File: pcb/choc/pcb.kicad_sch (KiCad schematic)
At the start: 144 parts, among them J1 MJ-4PP-9, J10 Conn_01x08_Female, J2 USB_C_Receptacle_USB2.0, J3 Conn_01x12_Female, J4 Conn_01x04_Female, J5 Conn_01x08_Female, J6 MJ-4PP-9, J7 USB_C_Receptacle_USB2.0, J8 Conn_01x12_Female, J9 Conn_01x04_Female, SW1 SW_PUSH, SW10 SW_PUSH, SW11 SW_PUSH, SW12 SW_PUSH, SW13 SW_PUSH, SW14 SW_PUSH, SW15 SW_PUSH, SW16 SW_PUSH, SW17 SW_PUSH, SW18 SW_PUSH, SW19 SW_PUSH, SW2 SW_PUSH, SW20 SW_PUSH, SW21 SW_PUSH, SW22 SW_PUSH, SW23 SW_PUSH, SW24 SW_PUSH, SW25 SW_PUSH, SW26 SW_PUSH, SW27 SW_PUSH, SW28 SW_PUSH, SW29 SW_PUSH, SW3 SW_PUSH, SW30 SW_PUSH, SW31 SW_PUSH, SW32 SW_PUSH, SW33 SW_PUSH, SW34 SW_PUSH, SW35 SW_PUSH, SW36 SW_PUSH, SW37 SW_PUSH, SW38 SW_PUSH, SW4 SW_PUSH, SW5 SW_PUSH, SW6 SW_PUSH, SW7 SW_PUSH, SW8 SW_PUSH, SW9 SW_PUSH, U1 rp2040-zero, U2 rp2040-zero, U3 roller, U4 roller

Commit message: draft 1
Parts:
- added BR1, BR2, BR3, BR4: MountingHole, zzkeeb:Hole_Breakaway-Tabs, symbol Mechanical:MountingHole
- added CIRQUE2, CIRQUE4: Conn_01x12_Female, zzkeeb:Connector_FPC-FFC-adapter-12pin, symbol zzkeeb:Pointing_Cirque
- CIRQUE1: renamed from J3; footprint (none) -> zzkeeb:Connector_FFC-FPC-vertical-12pin; symbol Connector:Conn_01x12_Female -> zzkeeb:Pointing_Cirque
- CIRQUE3: renamed from J8; footprint (none) -> zzkeeb:Connector_FFC-FPC-vertical-12pin; symbol Connector:Conn_01x12_Female -> zzkeeb:Pointing_Cirque
- DISP1: renamed from J5; footprint Connector_JST:JST_PH_S8B-PH-K_1x08_P2.00mm_Horizontal -> zzkeeb:Connector_JST_PH_S8B-PH-K_1x08_P2.00mm_Horizontal; symbol Connector:Conn_01x08_Female -> zzkeeb:Display_Waveshare
- DISP2: renamed from J10; footprint Connector_JST:JST_PH_S8B-PH-K_1x08_P2.00mm_Horizontal -> zzkeeb:Connector_JST_PH_S8B-PH-K_1x08_P2.00mm_Horizontal; symbol Connector:Conn_01x08_Female -> zzkeeb:Display_Waveshare
- I2C1: renamed from J4; symbol Connector:Conn_01x04_Female -> zzkeeb:Pointing_Circue-adapter
- I2C2: renamed from J9; symbol Connector:Conn_01x04_Female -> zzkeeb:Pointing_Circue-adapter
- LED1, LED10, LED11, LED12, LED13, LED14, LED15, LED16, LED17, LED18, LED19, LED2, LED20, LED21, LED22, LED23, LED24, LED25, LED26, LED27, LED28, LED29, LED3, LED30, LED31, LED32, LED33, LED34, LED35, LED36, LED37, LED38, LED4, LED5, LED6, LED7, LED8, LED9: symbol kbd:YS-SK6812MINI-E -> zzkeeb:LED_SK6812MINI-E
- MCU1: renamed from U1; symbol kleeb-mcu:rp2040-zero -> zzkeeb:MCU_rp2040-zero
- MCU2: renamed from U2; symbol kleeb-mcu:rp2040-zero -> zzkeeb:MCU_rp2040-zero
- SW1, SW10, SW11, SW12, SW13, SW14, SW15, SW16, SW17, SW18, SW19, SW2, SW20, SW21, SW22, SW23, SW24, SW25, SW26, SW27, SW28, SW29, SW3, SW30, SW31, SW32, SW33, SW34, SW35, SW36, SW37, SW38, SW4, SW5, SW6, SW7, SW8, SW9: value SW_PUSH -> Switch; symbol kbd:SW_PUSH -> zzkeeb:Switch
- TRRS1: renamed from J1; symbol kbd:MJ-4PP-9 -> Connector:AudioJack4
- TRRS2: renamed from J6; symbol kbd:MJ-4PP-9 -> Connector:AudioJack4
- renumbered U3 to ROLL1, U4 to ROLL2, J2 to USB1, J7 to USB2
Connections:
- net CS: now also CIRQUE1.10 (SS), MCU1.10 (9), CIRQUE2.10 (SS); no longer CIRQUE1.11 (Pin_11), MCU1.6 (5)
- net CS_r: now also CIRQUE3.10 (SS), MCU2.10 (9), CIRQUE4.10 (SS); no longer CIRQUE3.11 (Pin_11), MCU2.6 (5)
- net GND: now also TRRS1.R1, CIRQUE2.2 (GND); no longer TRRS1.C
- net GNDA: now also TRRS2.R1, CIRQUE4.2 (GND); no longer TRRS2.C
- net MISO/DC: now also CIRQUE1.11 (MISO), MCU1.13 (12), CIRQUE2.11 (MISO); no longer CIRQUE1.10 (Pin_10), MCU1.5 (4)
- net MISO/DC_r: now also CIRQUE3.11 (MISO), MCU2.13 (12), CIRQUE4.11 (MISO); no longer CIRQUE3.10 (Pin_10), MCU2.5 (4)
- net MOSI/SCL: now also MCU1.12 (11), CIRQUE2.4 (SCL), CIRQUE2.8 (MOSI); no longer MCU1.4 (3)
- net MOSI/SCL_r: now also MCU2.12 (11), CIRQUE4.4 (SCL), CIRQUE4.8 (MOSI); no longer MCU2.4 (3)
- net RST: now also MCU1.14 (13); no longer MCU1.7 (6)
- net RST_r: now also MCU2.14 (13); no longer MCU2.7 (6)
- net RX: now also TRRS1.T; no longer TRRS1.B
- net RX_r: now also TRRS2.T; no longer TRRS2.B
- net SCLK/SDA: now also MCU1.11 (10), CIRQUE2.12 (SCK), CIRQUE2.3 (SDA); no longer MCU1.3 (2)
- net SCLK/SDA_r: now also MCU2.11 (10), CIRQUE4.12 (SCK), CIRQUE4.3 (SDA); no longer MCU2.3 (2)
- net TX: now also TRRS1.S; no longer TRRS1.A
- net TX_r: now also TRRS2.S; no longer TRRS2.A
- net VCC: now also TRRS1.R2, CIRQUE2.1 (3V3); no longer TRRS1.D
- net VDD: now also TRRS2.R2, CIRQUE4.1 (3V3); no longer TRRS2.D
- net col0: now also MCU1.3 (2); no longer MCU1.10 (9)
- net col0_r: now also MCU2.3 (2); no longer MCU2.10 (9)
- net col1: now also MCU1.4 (3); no longer MCU1.11 (10)
- net col1_r: now also MCU2.4 (3); no longer MCU2.11 (10)
- net col2: now also MCU1.5 (4); no longer MCU1.12 (11)
- net col2_r: now also MCU2.5 (4); no longer MCU2.12 (11)
- net col3: now also MCU1.6 (5); no longer MCU1.13 (12)
- net col3_r: now also MCU2.6 (5); no longer MCU2.13 (12)
- net col4: now also MCU1.7 (6); no longer MCU1.14 (13)
- net col4_r: now also MCU2.7 (6); no longer MCU2.14 (13)
- net row0: now also MCU1.18 (27); no longer MCU1.15 (14)
- net row0_r: now also MCU2.18 (27); no longer MCU2.15 (14)
- net row1: now also MCU1.17 (26); no longer MCU1.16 (15)
- net row1_r: now also MCU2.17 (26); no longer MCU2.16 (15)
- net row2: now also MCU1.16 (15); no longer MCU1.17 (26)
- net row2_r: now also MCU2.16 (15); no longer MCU2.17 (26)
- net row3: now also MCU1.15 (14); no longer MCU1.18 (27)
- net row3_r: now also MCU2.15 (14); no longer MCU2.18 (27)
- no-connect marks 24 -> 32
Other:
- moved on the sheet: H1, H10, H11, H12, H2, H3, H4, H5, H6, H7, H8, H9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

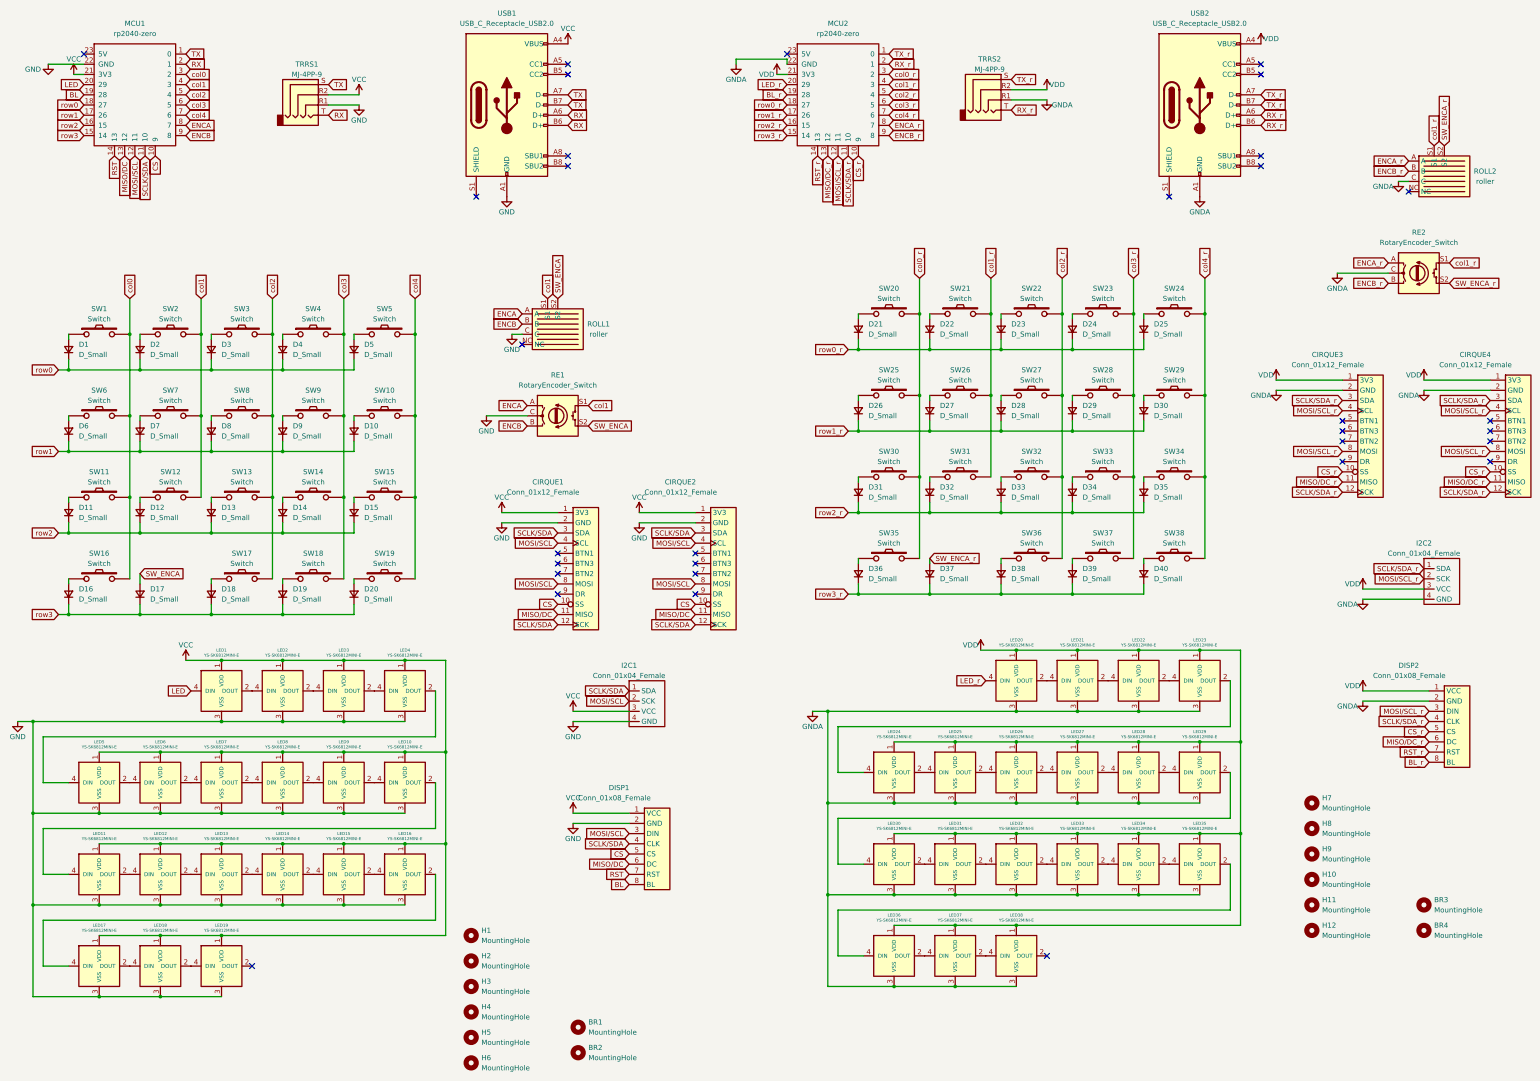
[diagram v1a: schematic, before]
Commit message: component placement
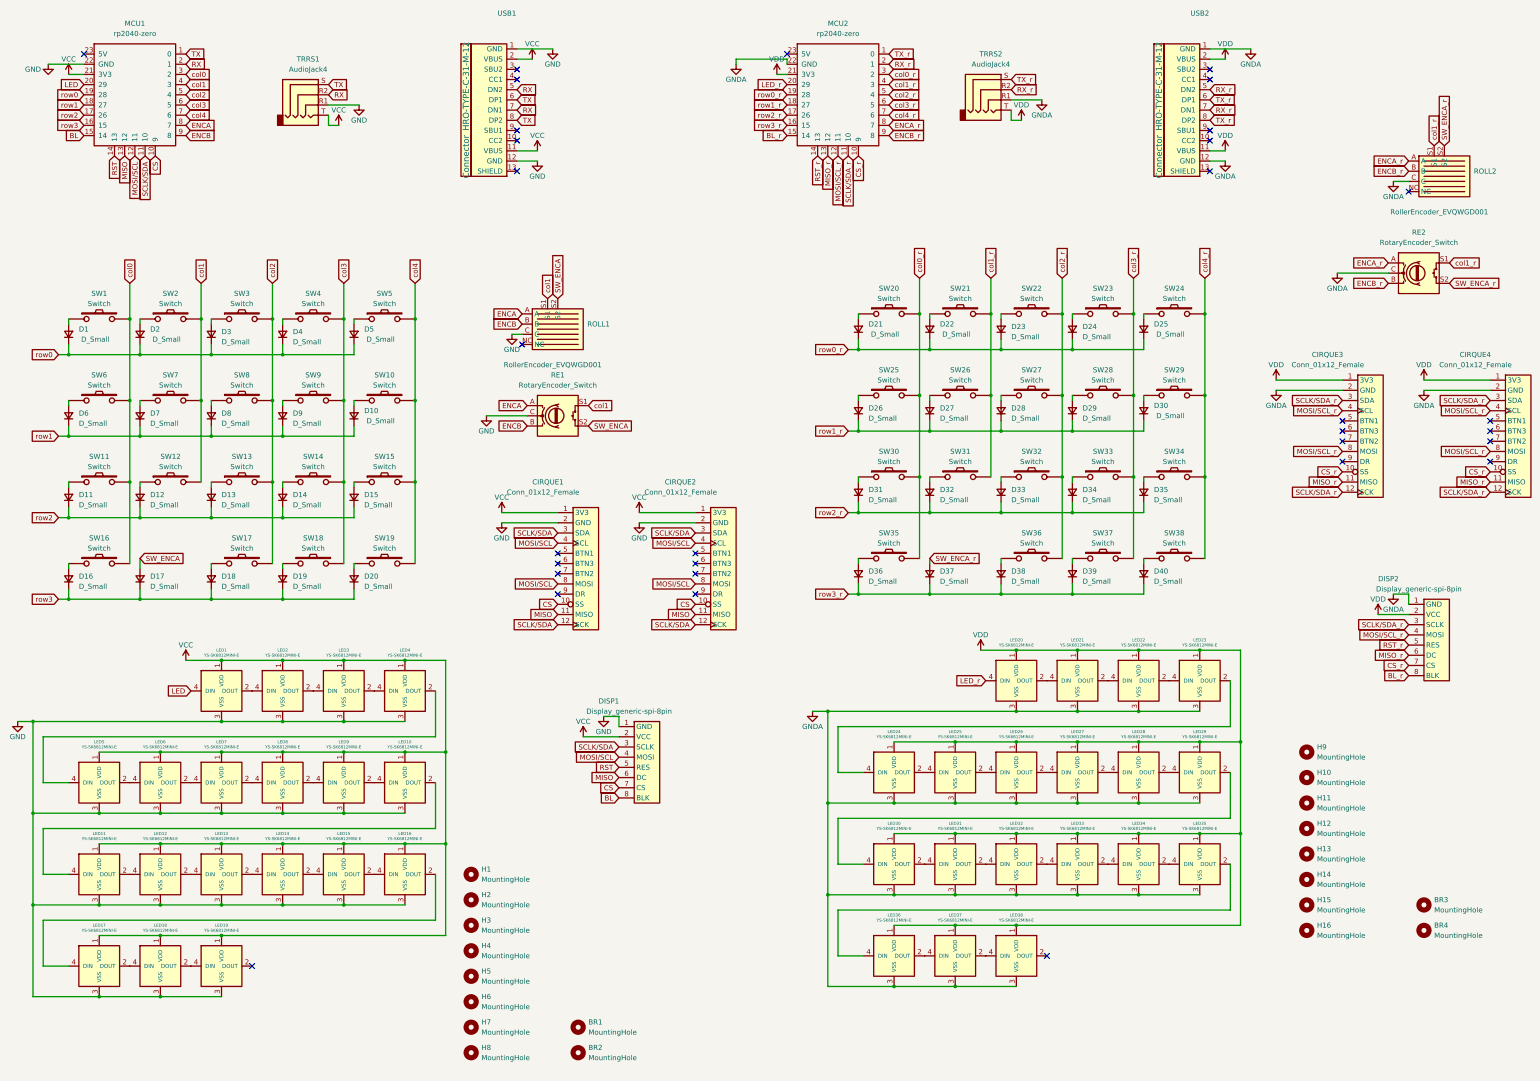
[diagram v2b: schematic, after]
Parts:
- removed I2C1, I2C2: Conn_01x04_Female, zzkeeb:Pointing_Cirque-adapter, symbol zzkeeb:Pointing_Circue-adapter
- added H13, H14, H15, H16: MountingHole, zzkeeb:Hole_M2-spacer, symbol Mechanical:MountingHole
- DISP1, DISP2: value Conn_01x08_Female -> Display_generic-spi-8pin; footprint zzkeeb:Connector_JST_PH_S8B-PH-K_1x08_P2.00mm_Horizontal -> zzkeeb:Connector_Display-8pin-SPI-2.0mm; symbol zzkeeb:Display_Waveshare -> zzkeeb:Display_generic-spi-8pin
- ROLL1, ROLL2: value roller -> RollerEncoder_EVQWGD001
- TRRS1, TRRS2: value MJ-4PP-9 -> AudioJack4; symbol Connector:AudioJack4 -> Connector_Audio:AudioJack4
- USB1, USB2: value USB_C_Receptacle_USB2.0 -> Connector_HRO-TYPE-C-31-M-12; footprint zzkeeb:Connector_USB-C-mid-mount-ali-data -> zzkeeb:Connector_HRO-TYPE-C-31-M-12-data; symbol Connector:USB_C_Receptacle_USB2.0 -> zzkeeb:Connector_HRO-TYPE-C-31-M-12
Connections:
- net BL: now also MCU1.15 (14); no longer MCU1.19 (28)
- net BL_r: now also MCU2.15 (14); no longer MCU2.19 (28)
- net CS: now also DISP1.7 (CS); no longer DISP1.5 (CS)
- net CS_r: now also DISP2.7 (CS); no longer DISP2.5 (CS)
- net GND: now also DISP1.1 (GND), USB1.1 (GND), USB1.12 (GND); no longer DISP1.2 (GND), USB1.A1 (GND), USB1.A12 (GND), USB1.B1 (GND), USB1.B12 (GND)
- net GNDA: now also DISP2.1 (GND), USB2.1 (GND), USB2.12 (GND); no longer DISP2.2 (GND), USB2.A1 (GND), USB2.A12 (GND), USB2.B1 (GND), USB2.B12 (GND)
- net MOSI/SCL: now also DISP1.4 (MOSI); no longer DISP1.3 (DIN)
- net MOSI/SCL_r: now also DISP2.4 (MOSI); no longer DISP2.3 (DIN)
- net RST: now also DISP1.5 (RES); no longer DISP1.7 (RST)
- net RST_r: now also DISP2.5 (RES); no longer DISP2.7 (RST)
- net RX: now also TRRS1.R2, USB1.5 (DN2), USB1.7 (DN1); no longer TRRS1.T, USB1.A6 (D+), USB1.B6 (D+)
- net RX_r: now also TRRS2.R2, USB2.5 (DN2), USB2.7 (DN1); no longer TRRS2.T, USB2.A6 (D+), USB2.B6 (D+)
- net SCLK/SDA: now also DISP1.3 (SCLK); no longer DISP1.4 (CLK)
- net SCLK/SDA_r: now also DISP2.3 (SCLK); no longer DISP2.4 (CLK)
- net TX: now also USB1.6 (DP1), USB1.8 (DP2); no longer USB1.A7 (D-), USB1.B7 (D-)
- net TX_r: now also USB2.6 (DP1), USB2.8 (DP2); no longer USB2.A7 (D-), USB2.B7 (D-)
- net VCC: now also DISP1.2 (VCC), TRRS1.T, USB1.11 (VBUS), USB1.2 (VBUS); no longer DISP1.1 (VCC), TRRS1.R2, USB1.A4 (VBUS), USB1.A9 (VBUS), USB1.B4 (VBUS), USB1.B9 (VBUS)
- net VDD: now also DISP2.2 (VCC), TRRS2.T, USB2.11 (VBUS), USB2.2 (VBUS); no longer DISP2.1 (VCC), TRRS2.R2, USB2.A4 (VBUS), USB2.A9 (VBUS), USB2.B4 (VBUS), USB2.B9 (VBUS)
- net row0: now also MCU1.19 (28); no longer MCU1.18 (27)
- net row0_r: now also MCU2.19 (28); no longer MCU2.18 (27)
- net row1: now also MCU1.18 (27); no longer MCU1.17 (26)
- net row1_r: now also MCU2.18 (27); no longer MCU2.17 (26)
- net row2: now also MCU1.17 (26); no longer MCU1.16 (15)
- net row2_r: now also MCU2.17 (26); no longer MCU2.16 (15)
- net row3: now also MCU1.16 (15); no longer MCU1.15 (14)
- net row3_r: now also MCU2.16 (15); no longer MCU2.15 (14)
- net MISO/DC renamed MISO
- net MISO/DC_r renamed MISO_r
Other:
- moved on the sheet: D1, D10, D11, D12, D13, D14, D15, D16, D17, D18, D19, D2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
